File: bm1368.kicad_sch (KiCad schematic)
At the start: 52 parts, among them U1 25MHz, U14 BM1366_mode1, U2 TXB0104RGYR, U5 MCP1824T-1802E, U6 MCP1824T-0802E

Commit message: schematic title update
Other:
- title: Bitaxe Ultra -> Bitaxe Supra
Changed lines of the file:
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@@
   (paper "A")
   (title_block
-    (title "Bitaxe Ultra")
-    (date "2023-12-15")
-    (rev "205")
+    (title "Bitaxe Supra")
+    (date "2024-02-14")
+    (rev "401")
   )
   (junction (at 120.015 46.355) (diameter 0) (color 0 0 0 0)

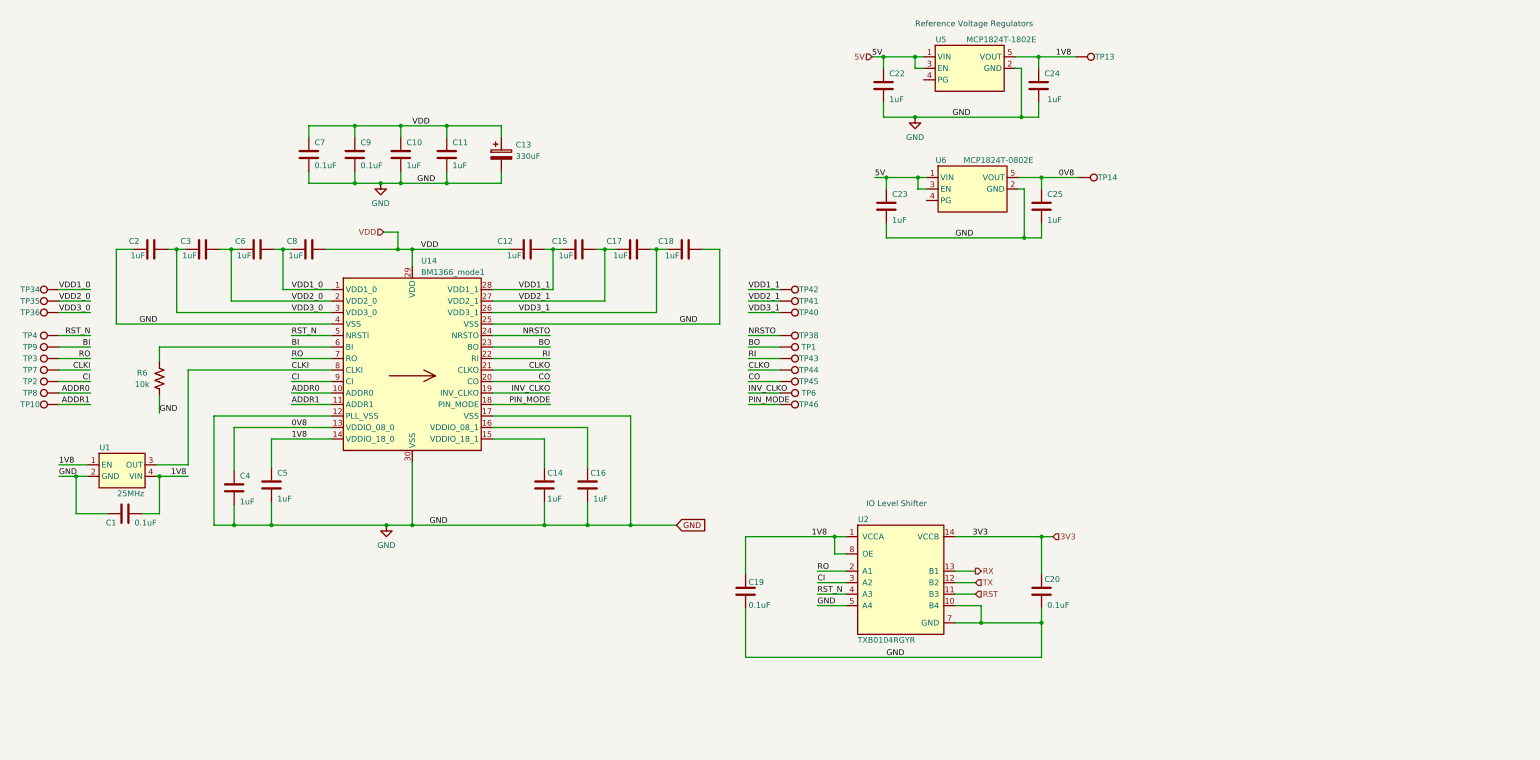
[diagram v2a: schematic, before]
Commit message: mostly merged. some track cleanup needed
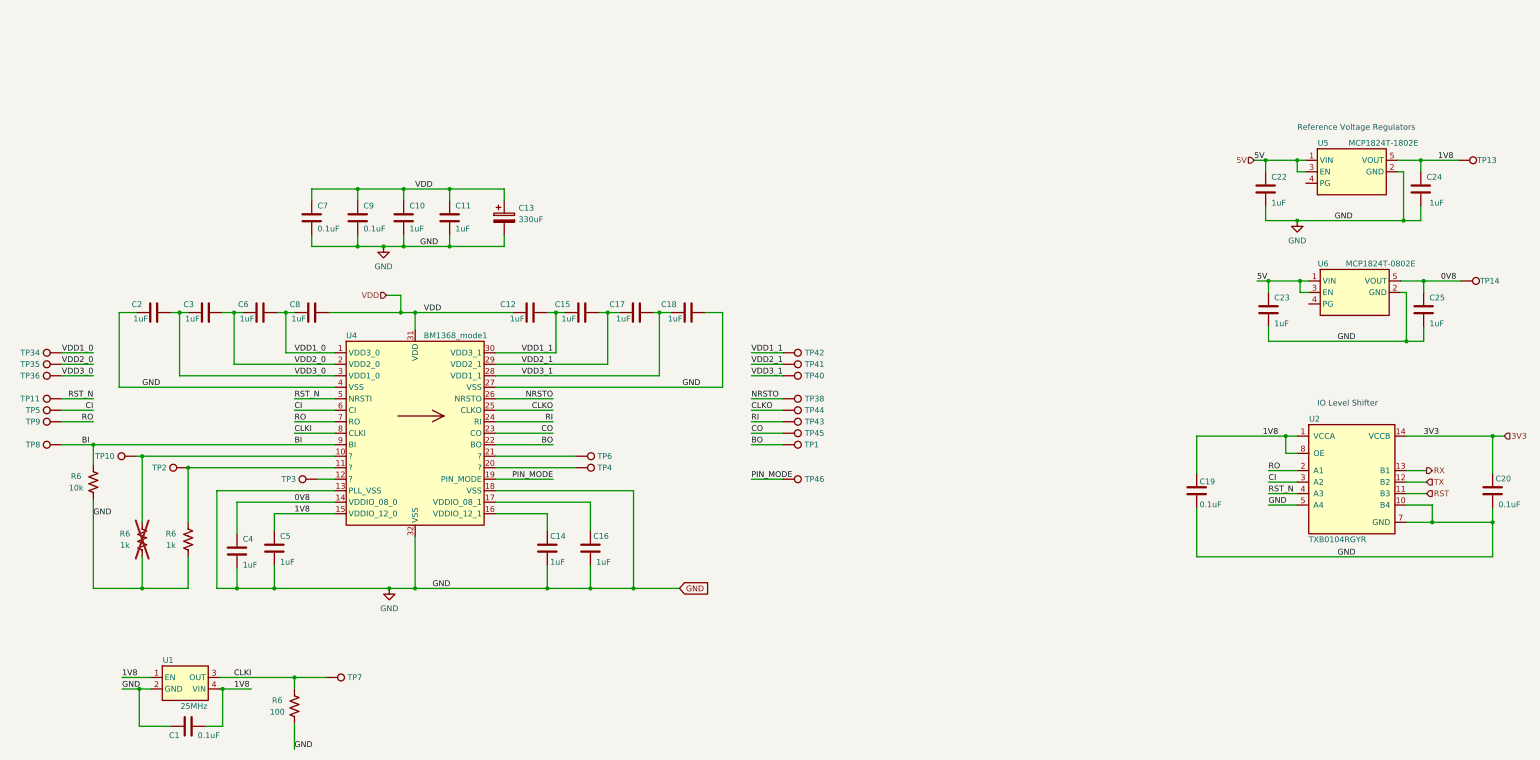
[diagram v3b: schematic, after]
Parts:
- removed R6: 10k, Resistor_SMD:R_0402_1005Metric, symbol Device:R_US
- removed U14: BM1366_mode1, bitaxe:BM1366, symbol bitaxe:BM1366_mode1
- added R6 (x2): 1k, Resistor_SMD:R_0402_1005Metric, symbol Device:R_US
- added R6: 100, Resistor_SMD:R_0402_1005Metric, symbol Device:R_US
- added R6: 10k, Resistor_SMD:R_0402_1005Metric, symbol Device:R_US
- added TP11, TP5: TestPoint, TestPoint:TestPoint_Pad_D1.5mm, symbol Connector:TestPoint
- added U4: BM1368_mode1, bitaxe:BM1368, symbol bitaxe:BM1368_mode1
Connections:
- net ADDR0 is gone; now on net BI: TP8.1
- net 0V8: now also U4.14 (VDDIO_08_0)
- net 1V8: now also U4.15 (VDDIO_12_0)
- net BI: now also R6.2, U4.9 (BI); no longer TP9.1
- net BO: now also U4.22 (BO)
- net CI: now also TP5.1, U4.6 (CI); no longer TP2.1
- net CLKI: now also R6.2, U4.8 (CLKI)
- net CLKO: now also U4.25 (CLKO)
- net CO: now also U4.23 (CO)
- net GND: now also R6.1, R6.1, R6.1, R6.1, U4.13 (PLL_VSS), U4.18 (VSS), U4.27 (VSS), U4.32 (VSS), U4.4 (VSS)
- net NRSTO: now also U4.26 (NRSTO)
- net PIN_MODE: now also U4.19 (PIN_MODE)
- net RI: now also U4.24 (RI)
- net RO: now also TP9.1, U4.7 (RO); no longer TP3.1
- net RST_N: now also TP11.1, U4.5 (NRSTI); no longer TP4.1
- net VDD: now also U4.31 (VDD)
- net VDD1_0: now also U4.1 (VDD3_0)
- net VDD1_1: now also U4.30 (VDD3_1)
- net VDD2_0: now also U4.2 (VDD2_0)
- net VDD2_1: now also U4.29 (VDD2_1)
- net VDD3_0: now also U4.3 (VDD1_0)
- net VDD3_1: now also U4.28 (VDD1_1)
- net at C14.1: now also U4.16 (VDDIO_12_1)
- net at C16.1: now also U4.17 (VDDIO_08_1)
- net ADDR1: no longer names the net of TP10.1
- net ADDR1: now also R6.2, U4.10 (?)
- net INV_CLKO: no longer names the net of TP6.1
- net INV_CLKO: now also U4.21 (?)
- new net: R6.2, TP2.1, U4.11 (?)
- new net: TP3.1, U4.12 (?)
- new net: TP4.1, U4.20 (?)
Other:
- moved on the sheet: C19, C20, C22, C23, C24, C25, TP13, TP14, U2, U5, U6

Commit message: track cleanup, added BOM
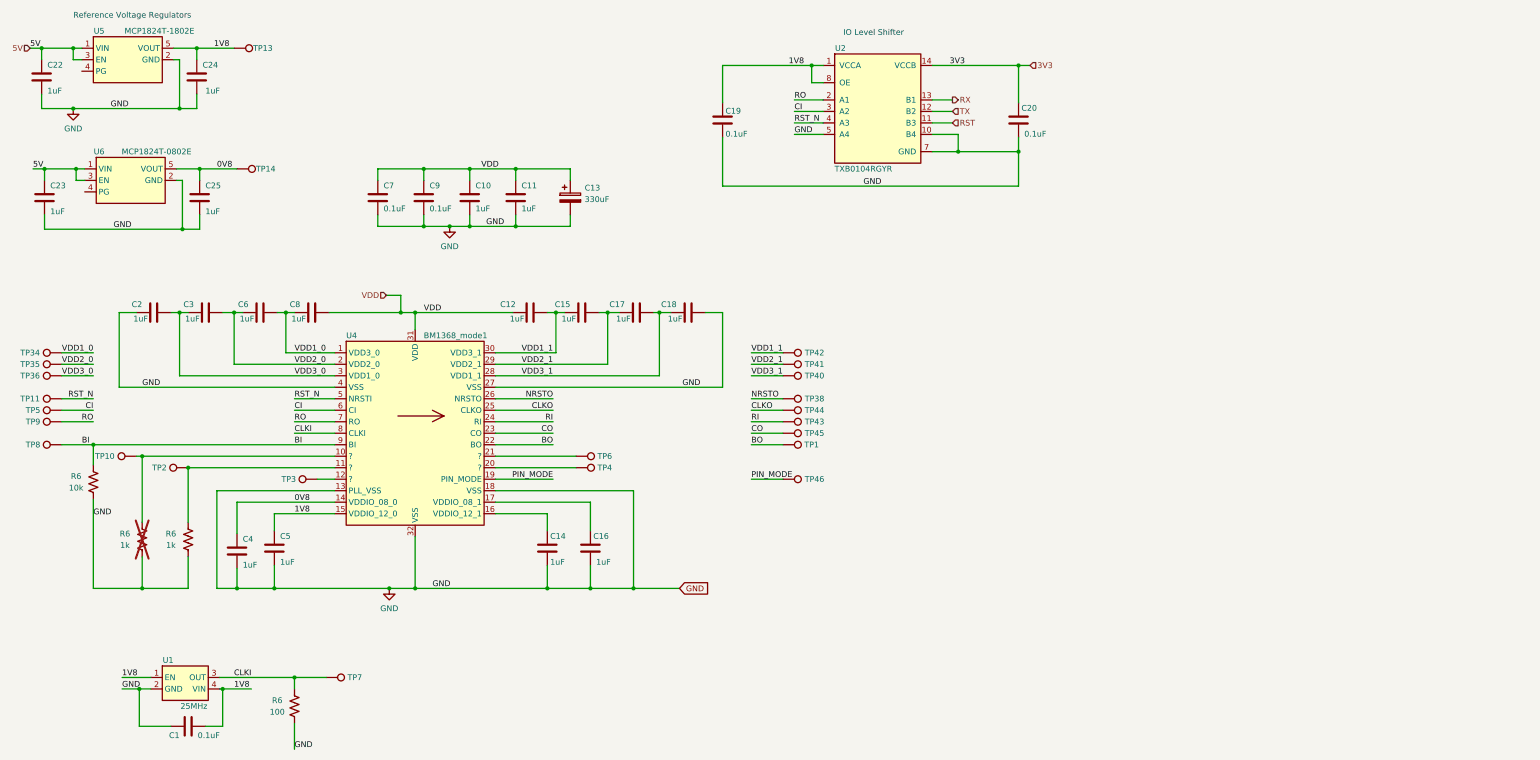
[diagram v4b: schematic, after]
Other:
- title: Bitaxe Supra -> bitaxeSupra
- moved on the sheet: C10, C11, C13, C19, C20, C22, C23, C24, C25, C7, C9, TP13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

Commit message: renamed and deleted everything except pogo pads
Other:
- title: bitaxeSupra -> axeTester
